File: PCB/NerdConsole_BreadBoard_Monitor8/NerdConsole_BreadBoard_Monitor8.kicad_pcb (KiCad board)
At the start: 2 copper layers, 15.8 x 25 mm, 11 parts, among them J1 Conn_01x09, J2 Conn_01x09

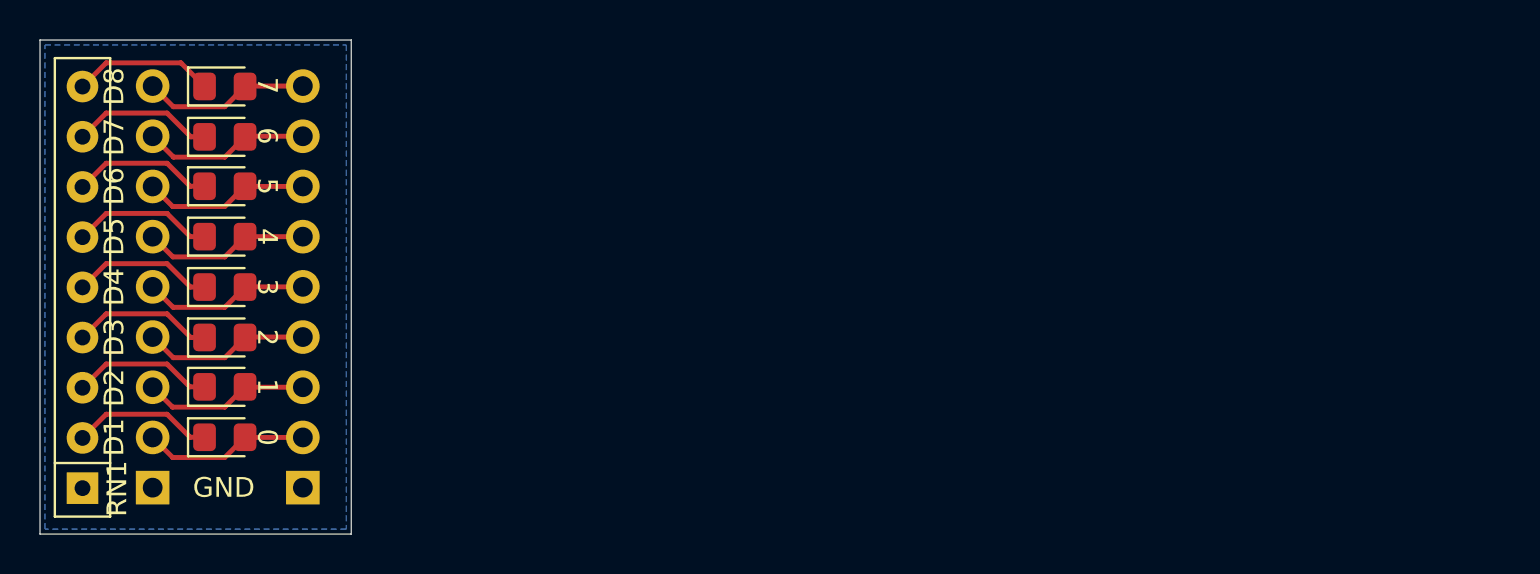
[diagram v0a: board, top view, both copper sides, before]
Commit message: Renamed Monitor to BridgeMonitor and made a new free standing Monitor.
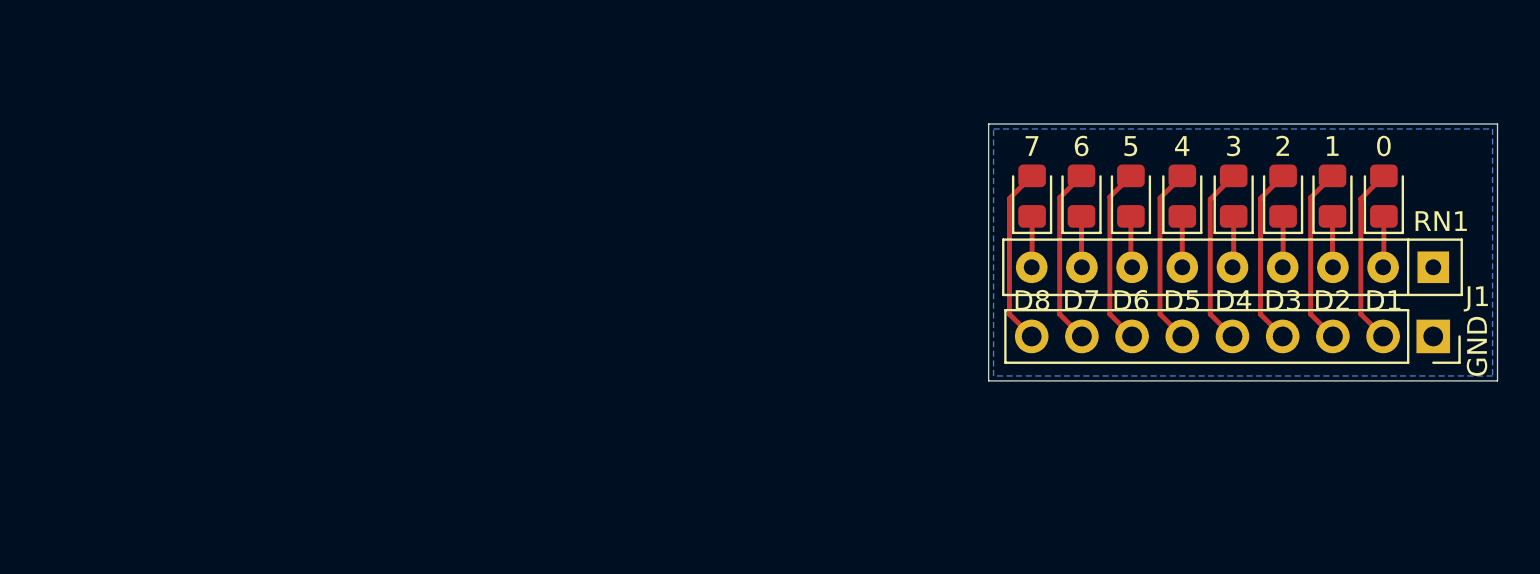
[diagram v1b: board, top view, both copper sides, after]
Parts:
- removed J2: Conn_01x09, Connector_PinHeader_2.54mm:PinHeader_1x09_P2.54mm_Vertical
- J1: footprint Connector_PinHeader_2.54mm:PinHeader_1x09_P2.54mm_Vertical -> Connector_PinSocket_2.54mm:PinSocket_1x09_P2.54mm_Vertical; moved to F.Cu
- RN1: value 1K -> R_Network08_US
- moved RN1 69.3 mm to (161.0, 87.0), turned to 180 degrees
- moved J1 65.2 mm to (161.0, 90.5), turned to 270 degrees
- moved D1 59.9 mm to (158.5, 83.4), turned to 90 degrees
- moved D2 56.9 mm to (155.9, 83.4), turned to 90 degrees
- moved D3 54.0 mm to (153.4, 83.4), turned to 90 degrees
- moved D4 51.3 mm to (150.9, 83.4), turned to 90 degrees
- moved D5 48.5 mm to (148.3, 83.4), turned to 90 degrees
- moved D6 45.9 mm to (145.7, 83.4), turned to 90 degrees
- moved D7 43.5 mm to (143.2, 83.4), turned to 90 degrees
- moved D8 41.2 mm to (140.7, 83.4), turned to 90 degrees
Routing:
- net LED6: track 7.17 -> 2.58 mm
- net LED4: track 7.16 -> 2.58 mm
- net LED7: track 7.17 -> 2.58 mm
- net LED2: track 7.17 -> 2.58 mm
- net LED1: track 7.15 -> 2.58 mm
- net LED3: track 7.16 -> 2.60 mm
- net LED0: track 7.15 -> 2.59 mm
- net LED5: track 7.15 -> 2.60 mm
- net D3: track 8.46 -> 9.08 mm
- net D0: track 8.45 -> 9.07 mm
- net D4: track 8.45 -> 9.06 mm
- net D2: track 8.47 -> 9.07 mm
- net D1: track 8.45 -> 9.05 mm
- net D7: track 8.47 -> 9.07 mm
- net D5: track 8.45 -> 9.03 mm
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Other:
- board size 15.8 x 25 mm -> 25.8 x 13 mm

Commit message: Added NerdConsole labelling and a couple more boards.
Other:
- board text added: "NerdConsole BreadBoard Monitor 8 v1"
